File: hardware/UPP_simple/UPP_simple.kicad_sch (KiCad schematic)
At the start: 9 parts, among them IC2 STM32G0C1KCT6N

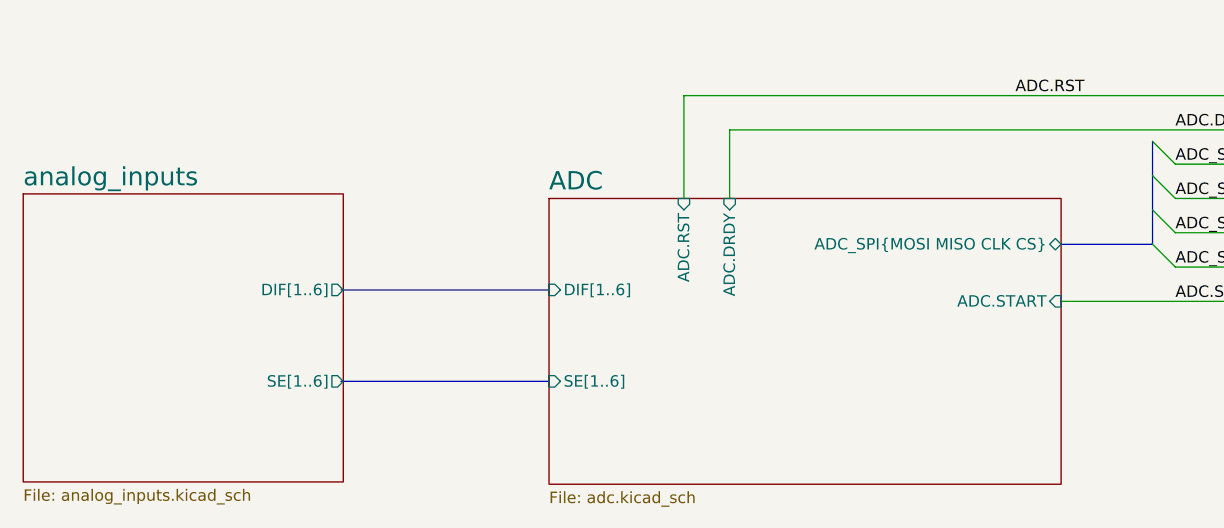
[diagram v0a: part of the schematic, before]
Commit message: Solved ERC errors and cleaned up schematic
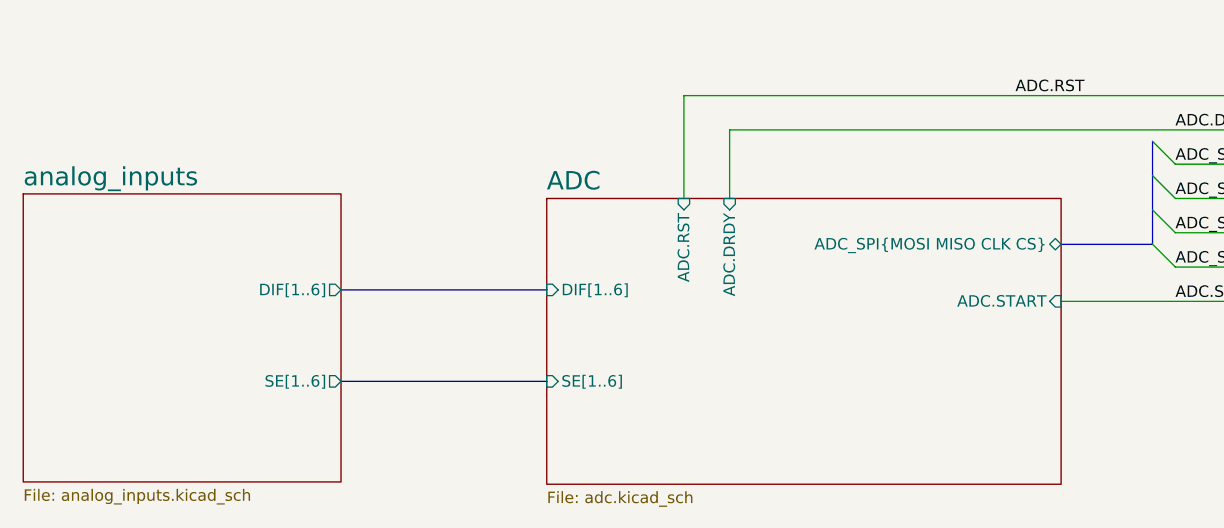
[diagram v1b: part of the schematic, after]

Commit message: Add files via upload
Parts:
- removed C9: 330n, Capacitor_SMD:C_0603_1608Metric_Pad1.08x0.95mm_HandSolder, symbol Device:C
- removed IC2: STM32G0C1KCT6N, QFP80P900X900X160-32N, symbol STM32G0C1KCT6N:STM32G0C1KCT6N
- added C10: 100n, symbol Device:C_Small
- added U4: STM32G0C1KCTxN, Package_QFP:LQFP-32_7x7mm_P0.8mm, symbol MCU_ST_STM32G0:STM32G0C1KCTxN
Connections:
- net 3V3: now also C10.2, U4.20 (VDD), U4.4 (VDD)
- net GND: now also C10.1, U4.5 (VSS)
- net at R14.1: now also U4.30 (PB6)
- net at R9.1: now also U4.15 (PB0)
- net at R13.1: now also U4.11 (PA4)
- net at R12.1: now also U4.12 (PA5)
- net at R11.1: now also U4.13 (PA6)
- net at R10.1: now also U4.14 (PA7)
- net at R15.1: now also U4.16 (PB1)
- net ADC_SPI.CS renamed ADC_SPI.NSS
- no-connect marks 23 -> 22
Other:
- sheet ADC ports: added ADC_SPI{MOSI MISO CLK NSS}; removed ADC_SPI{MOSI MISO CLK CS}
